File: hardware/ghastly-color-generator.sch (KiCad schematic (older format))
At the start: 11 parts, among them IC1 ATTINY45-P, K1 3pin_dmx, P1 Power_in, P2 isp_interface, U1 7805_oturpe, U2 SN75176B, Y1 Crystal

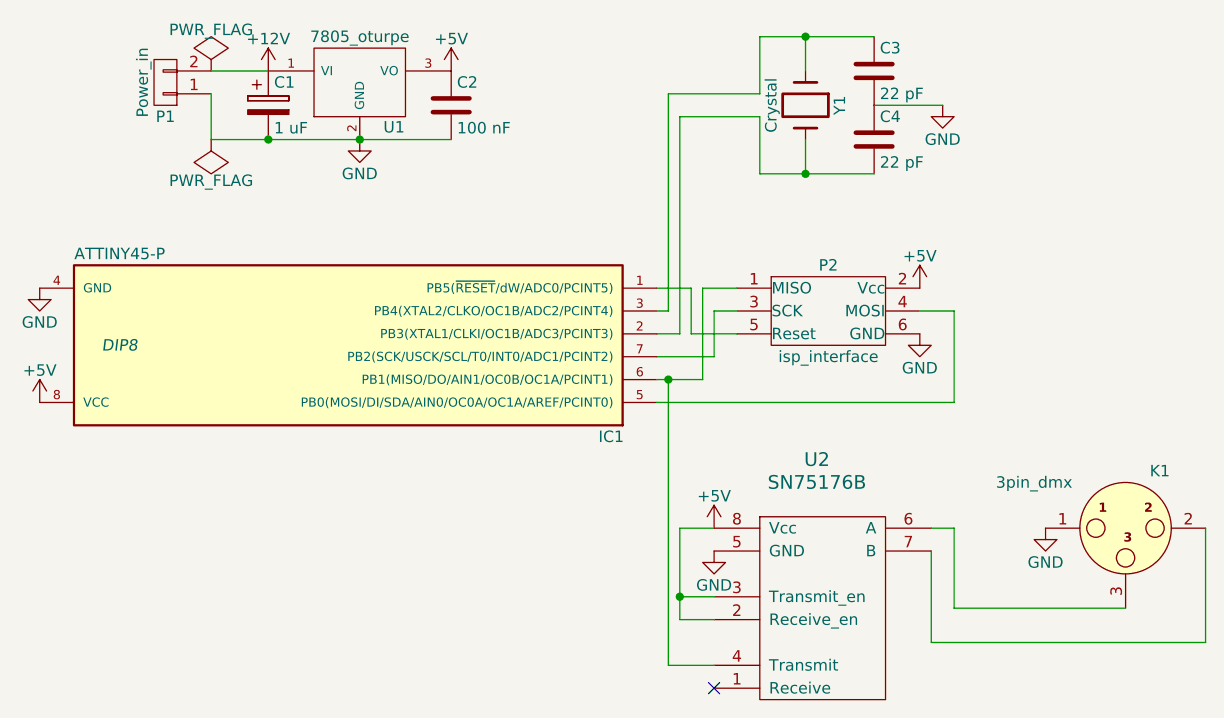
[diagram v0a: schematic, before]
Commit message: Add indicator to schematic
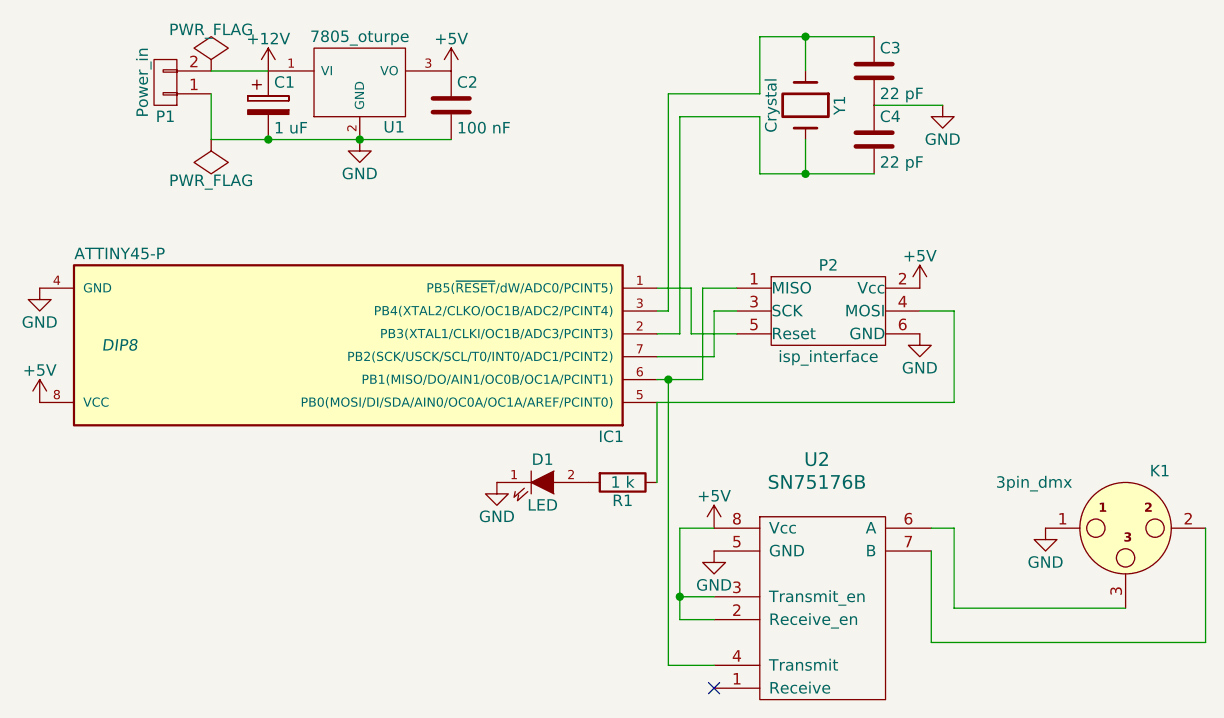
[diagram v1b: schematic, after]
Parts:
- added D1: LED, symbol LED
- added R1: 1 k, symbol R
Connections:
- net GND: now also D1.1 (K)
- net at IC1.5 (PB0(MOSI/DI/SDA/AIN0/OC0A/OC1A/AREF/PCINT0)), P2.4 (MOSI): now also R1.1
- new net: D1.2 (A), R1.2
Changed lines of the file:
@@
 LIBS:valves
 LIBS:oturpe-kicad-lib
+LIBS:ghastly-color-generator-cache
 EELAYER 25 0
 EELAYER END
@@
 $EndComp
 $Comp
-L GND #PWR01
+L GND #PWR1
 U 1 1 574C85A6
 P 2400 2950
-F 0 "#PWR01" H 2400 2700 50  0001 C CNN
+F 0 "#PWR1" H 2400 2700 50  0001 C CNN
 F 1 "GND" H 2400 2800 50  0000 C CNN
 F 2 "" H 2400 2950 50  0000 C CNN
@@
 $EndComp
 $Comp
-L +5V #PWR02
+L +5V #PWR2
 U 1 1 574C85BC
 P 2400 3450
-F 0 "#PWR02" H 2400 3300 50  0001 C CNN
+F 0 "#PWR2" H 2400 3300 50  0001 C CNN
 F 1 "+5V" H 2400 3590 50  0000 C CNN
 F 2 "" H 2400 3450 50  0000 C CNN
@@
 $EndComp
 $Comp
-L GND #PWR03
+L GND #PWR4
 U 1 1 574C861F
 P 3800 2300
-F 0 "#PWR03" H 3800 2050 50  0001 C CNN
+F 0 "#PWR4" H 3800 2050 50  0001 C CNN
 F 1 "GND" H 3800 2150 50  0000 C CNN
 F 2 "" H 3800 2300 50  0000 C CNN
@@
 $EndComp
 $Comp
-L +12V #PWR04
+L +12V #PWR3
 U 1 1 574C8637
 P 3400 2000
-F 0 "#PWR04" H 3400 1850 50  0001 C CNN
+F 0 "#PWR3" H 3400 1850 50  0001 C CNN
 F 1 "+12V" H 3400 2140 50  0000 C CNN
 F 2 "" H 3400 2000 50  0000 C CNN
@@
 $EndComp
 $Comp
-L +5V #PWR05
+L +5V #PWR5
 U 1 1 574C864F
 P 4200 2000
-F 0 "#PWR05" H 4200 1850 50  0001 C CNN
+F 0 "#PWR5" H 4200 1850 50  0001 C CNN
 F 1 "+5V" H 4200 2140 50  0000 C CNN
 F 2 "" H 4200 2000 50  0000 C CNN
@@
 $EndComp
 $Comp
-L GND #PWR06
+L GND #PWR11
 U 1 1 574C8951
 P 6350 2150
-F 0 "#PWR06" H 6350 1900 50  0001 C CNN
+F 0 "#PWR11" H 6350 1900 50  0001 C CNN
 F 1 "GND" H 6350 2000 50  0000 C CNN
 F 2 "" H 6350 2150 50  0000 C CNN
@@
 	5250 2950 5100 2950
 $Comp
-L +5V #PWR07
+L +5V #PWR9
 U 1 1 574C9365
 P 6250 2950
-F 0 "#PWR07" H 6250 2800 50  0001 C CNN
+F 0 "#PWR9" H 6250 2800 50  0001 C CNN
 F 1 "+5V" H 6250 3090 50  0000 C CNN
 F 2 "" H 6250 2950 50  0000 C CNN
@@
 $EndComp
 $Comp
-L GND #PWR08
+L GND #PWR10
 U 1 1 574C9389
 P 6250 3150
-F 0 "#PWR08" H 6250 2900 50  0001 C CNN
+F 0 "#PWR10" H 6250 2900 50  0001 C CNN
 F 1 "GND" H 6250 3000 50  0000 C CNN
 F 2 "" H 6250 3150 50  0000 C CNN
@@
 $EndComp
 $Comp
-L GND #PWR09
+L GND #PWR8
 U 1 1 574C975B
 P 5350 4100
-F 0 "#PWR09" H 5350 3850 50  0001 C CNN
+F 0 "#PWR8" H 5350 3850 50  0001 C CNN
 F 1 "GND" H 5350 3950 50  0000 C CNN
 F 2 "" H 5350 4100 50  0000 C CNN
@@
 $EndComp
 $Comp
-L +5V #PWR010
+L +5V #PWR7
 U 1 1 574C9781
 P 5350 4000
-F 0 "#PWR010" H 5350 3850 50  0001 C CNN
+F 0 "#PWR7" H 5350 3850 50  0001 C CNN
 F 1 "+5V" H 5350 4140 50  0000 C CNN
 F 2 "" H 5350 4000 50  0000 C CNN
@@
 $EndComp
 $Comp
-L GND #PWR011
+L GND #PWR12
 U 1 1 574C9AE8
 P 6800 4000
-F 0 "#PWR011" H 6800 3750 50  0001 C CNN
+F 0 "#PWR12" H 6800 3750 50  0001 C CNN
 F 1 "GND" H 6800 3850 50  0000 C CNN
 F 2 "" H 6800 4000 50  0000 C CNN
@@
 Connection ~ 3400 2300
 $Comp
-L PWR_FLAG #FLG012
+L PWR_FLAG #FLG1
 U 1 1 574CA587
 P 3150 2000
-F 0 "#FLG012" H 3150 2095 50  0001 C CNN
+F 0 "#FLG1" H 3150 2095 50  0001 C CNN
 F 1 "PWR_FLAG" H 3150 2180 50  0000 C CNN
 F 2 "" H 3150 2000 50  0000 C CNN
@@
 $EndComp
 $Comp
-L PWR_FLAG #FLG013
+L PWR_FLAG #FLG2
 U 1 1 574CA69D
 P 3150 2300
-F 0 "#FLG013" H 3150 2395 50  0001 C CNN
+F 0 "#FLG2" H 3150 2395 50  0001 C CNN
 F 1 "PWR_FLAG" H 3150 2480 50  0000 C CNN
 F 2 "" H 3150 2300 50  0000 C CNN
@@
 	-1   0    0    1
 $EndComp
+$Comp
+L R R1
+U 1 1 574CBC76
+P 4950 3800
+F 0 "R1" V 5030 3800 50  0000 C CNN
+F 1 "1 k" V 4950 3800 50  0000 C CNN
+F 2 "" V 4880 3800 50  0000 C CNN
+F 3 "" H 4950 3800 50  0000 C CNN
+	1    4950 3800
+	0    1    1    0
+$EndComp
+$Comp
+L LED D1
+U 1 1 574CBD1D
+P 4600 3800
+F 0 "D1" H 4600 3900 50  0000 C CNN
+F 1 "LED" H 4600 3700 50  0000 C CNN
+F 2 "" H 4600 3800 50  0000 C CNN
+F 3 "" H 4600 3800 50  0000 C CNN
+	1    4600 3800
+	1    0    0    -1
+$EndComp
+$Comp
+L GND #PWR6
+U 1 1 574CBD60
+P 4400 3800
+F 0 "#PWR6" H 4400 3550 50  0001 C CNN
+F 1 "GND" H 4400 3650 50  0000 C CNN
+F 2 "" H 4400 3800 50  0000 C CNN
+F 3 "" H 4400 3800 50  0000 C CNN
+	1    4400 3800
+	1    0    0    -1
+$EndComp
+Wire Wire Line
+	5100 3450 5100 3800
 $EndSCHEMATC
